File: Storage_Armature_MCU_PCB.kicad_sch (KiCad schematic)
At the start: 58 parts, among them U4 TLV1117LV33DCYR

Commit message: VER1.0: сделал все питание и один измерительный канал
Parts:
- removed C65, C72: 1n, Capacitor_THT:C_Disc_D7.0mm_W2.5mm_P5.00mm, symbol Device:C_Small
- removed C70: 330u, Capacitor_THT:CP_Radial_D10.0mm_P5.00mm, symbol Device:C_Polarized_Small
- removed D21: URB2405ZP-10WR3, MORNSUN:URB_ZP-10WR3, symbol MORNSUN:URB_ZP-10WR3
- removed L3: (no value), Inductor_SMD:L_CommonModeChoke_Murata_DLW5BTMxxxSQ2x_5x5mm, symbol Device:L_Coupled_Small
- added C35, C45, C74: 10u, Capacitor_SMD:C_1206_3216Metric_Pad1.33x1.80mm_HandSolder, symbol Device:C_Small
- added C71, C73: 4.7u, Capacitor_SMD:C_1206_3216Metric_Pad1.33x1.80mm_HandSolder, symbol Device:C_Small
- added D1: B2405S-1WR3, MORNSUN:B_S-1WR3, symbol MORNSUN:B_S-1WR3
- added D10: SMCJ33A, Diode_SMD:D_SMC_Handsoldering, symbol Device:D_TVS
- added D23: (no value), LED_SMD:LED_0805_2012Metric, symbol Device:LED_Small
- added D9: WRB2403S-3WR2, MORNSUN:WRB_S-3WR2, symbol MORNSUN:WRB_S-3WR2
- added L2, L3: 6.8u, Inductor_SMD:L_1210_3225Metric_Pad1.42x2.65mm_HandSolder, symbol Device:L_Small
- added R58: 1.1k, Resistor_SMD:R_0805_2012Metric_Pad1.20x1.40mm_HandSolder, symbol Device:R_Small
- added U5: ADP3338AKCZ-3.3RL7, Package_TO_SOT_SMD:SOT-223-3_TabPin2, symbol Regulator_Linear:LM1117MP-3.3
- C68, C69: value 10u -> 4.7u
- D20: value (none) -> BZT52C10
- F1: value 0451002.MRL -> MF-SM075/60-2; footprint Fuse_my:SMD_2410 -> Fuse:Fuse_Bourns_MF-SM_7.98x5.44mm
- J6: footprint Connector_Molex:Molex_Mini-Fit_Jr_5566-04A_2x02_P4.20mm_Vertical -> Connector_Molex:Molex_Mini-Fit_Jr_5569-04A2_2x02_P4.20mm_Horizontal
- Q1: value (none) -> 20N06
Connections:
- net +24V: now also C67.1, C68.1, F1.2, C73.1, D10.1 (A1), L2.1, L3.1
- net +5V: now also D9.6 (+Vo)
- net -24V: now also D10.2 (A2)
- net GND: now also D9.7 (0V)
- net GNDD: now also C69.2, C71.2, C73.2, D1.1 (GND), D9.1 (GND)
- net GND_CAN: no longer J34.3 (Pin_3), J34.4 (Pin_4), J35.3 (Pin_3), J35.4 (Pin_4)
- net at C69.1: now also D9.2 (Vin), L3.2
- new net: C45.2, C74.1, D1.4 (+Vo), U5.3 (VI)
- new net: J34.3 (Pin_3), J34.4 (Pin_4), J35.3 (Pin_3), J35.4 (Pin_4)
- new net: D23.1 (K), R58.1
- new net: C71.1, D1.2 (Vin), L2.2
- new net +3.3V_ISO: C35.2, D23.2 (A), U5.2 (VO)
- new net GND_ISO: C35.1, C45.1, C74.2, D1.3 (0V), R58.2, U5.1 (GND)
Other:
- added sheet P_measure (Measure.kicad_sch)
- note added: "Защита 24В"
- note added: "Питание 3.3В отвязанное"
- note removed: "Защита от переполюсовки 24В"
- note removed: "НАДО ДОБАВИТЬ VRB2424LD-50WR3 / MORNSUN"
- moved on the sheet: C34, C44, C47, C48, C49, C66, C67, C68, C69, D11, D12, D14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

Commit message: VER1.0: разместил все компоненты
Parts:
- removed D15: (no value), Package_TO_SOT_SMD:SOT-23-3, symbol Power_Protection:ESDA5V3L
- removed H1, H4: MountingHole_Pad, MountingHole:MountingHole_4.3mm_M4_Pad_Via, symbol Mechanical:MountingHole_Pad
- added C65: 100n, Capacitor_SMD:C_0805_2012Metric_Pad1.18x1.45mm_HandSolder, symbol Device:C_Small
- added H4, H5: MountingHole, MountingHole:MountingHole_4.3mm_M4, symbol Mechanical:MountingHole
- added R47, R48: 20, Resistor_SMD:R_0805_2012Metric_Pad1.20x1.40mm_HandSolder, symbol Device:R_Small
- added U14: USBLC6-2P6, Package_TO_SOT_SMD:SOT-23-6, symbol Power_Protection:USBLC6-2SC6
- D5: Product Name BAS416 -> LBAT54HT1G
- J34, J35: footprint Connector_Molex:Molex_Mini-Fit_Jr_5566-04A_2x02_P4.20mm_Vertical -> Connector_Molex:Molex_Mini-Fit_Jr_5569-04A2_2x02_P4.20mm_Horizontal
- R1, R2: value 1k -> 10k
- U4: value TLV1117LV33DCYR -> ADP3338AKCZ-3.3RL7
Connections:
- net CAN1_RXD_MCU is gone; now on net CAN_RXD_MCU: D12.1 (RXD)
- net CAN1_TXD_MCU is gone; now on net CAN_TXD_MCU: D12.2 (TXD)
- net +3.3V: now also U14.5 (VBUS)
- net GND: now also C65.1, U14.2 (GND)
- net GND_CAN: now also J34.3 (Pin_3), J34.4 (Pin_4), J35.3 (Pin_3), J35.4 (Pin_4)
- net NRST: now also C65.2
- net SWCLK: now also U14.1 (I/O1); no longer J1.2 (Pin_2)
- net SWDIO: now also U14.3 (I/O2); no longer J1.3 (Pin_3)
- net CAN_RXD_MCU: now reaches U1.44 (PA11)
- net CAN_TXD_MCU: now reaches U1.45 (PA12)
- new net: R47.1, U14.4 (I/O2)
- new net: R48.1, U14.6 (I/O1)
- new net: J1.2 (Pin_2), R48.2
- new net: J1.3 (Pin_3), R47.2
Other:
- sheet P_measure renamed Sensor_1
- added sheet Sensor_2 (Measure.kicad_sch)
- added sheet Sensor_3 (Measure.kicad_sch)
- added sheet Sensor_4 (Measure.kicad_sch)
- added sheet Sensor_5 (Measure.kicad_sch)
- note removed: "НВЦТ.0001.0400.200_v1"
- note removed: "Разъемы и механические отверстия"
- title: Плата управления -> Плата управления арматурой 
- moved on the sheet: C26, C30, C34, C44, R1, Y1

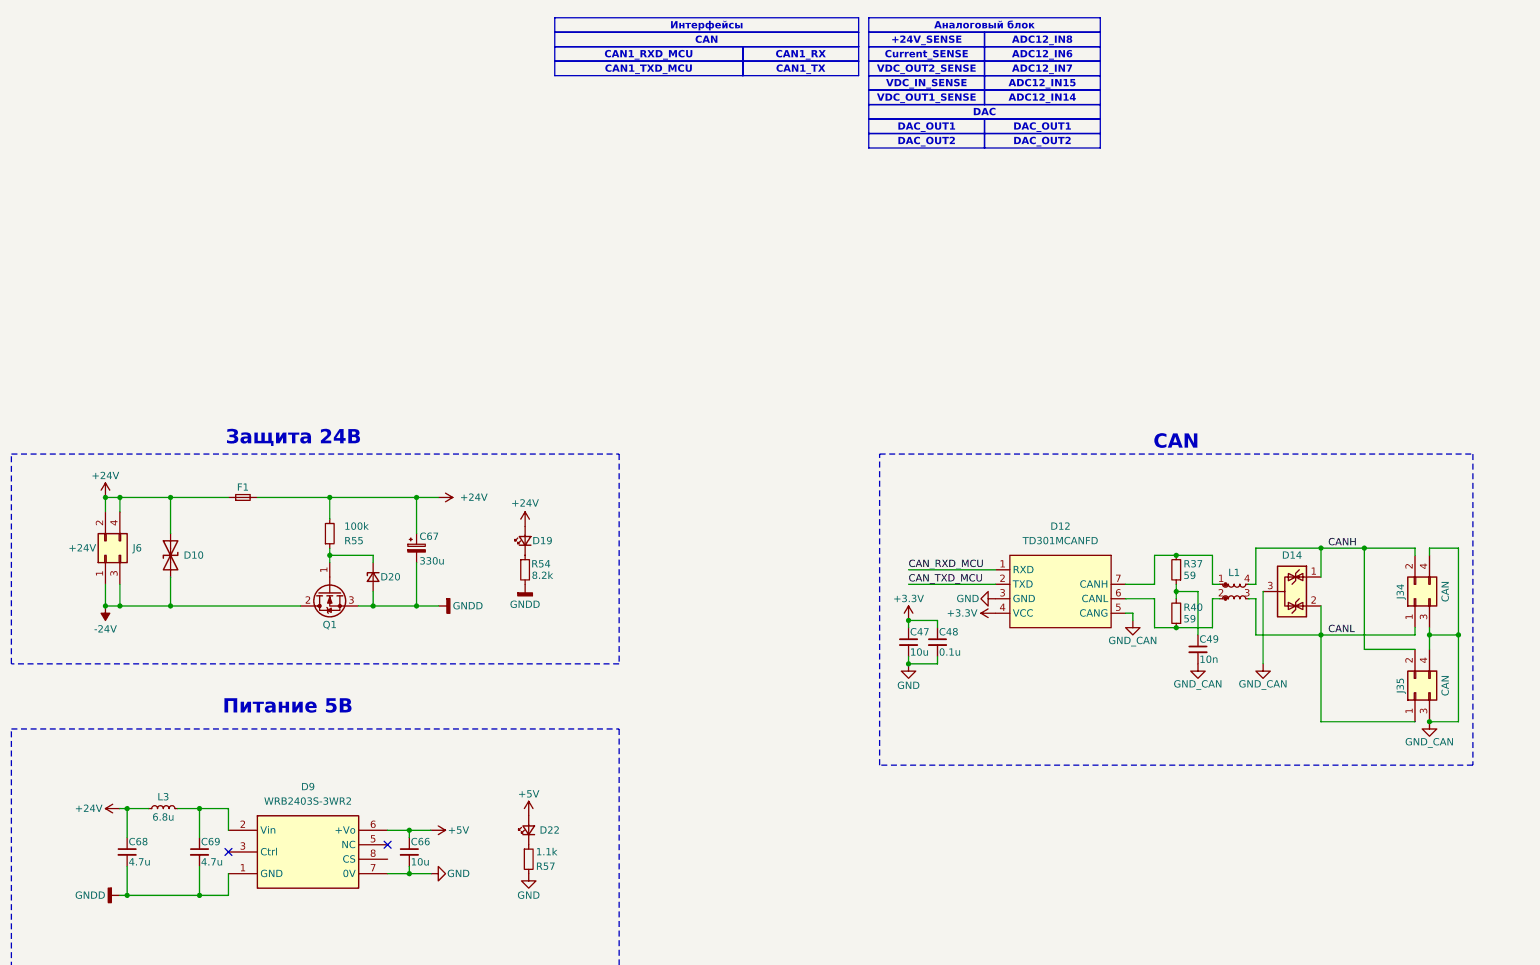
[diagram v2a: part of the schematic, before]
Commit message: VER1.0: развел все кроме ножек МК
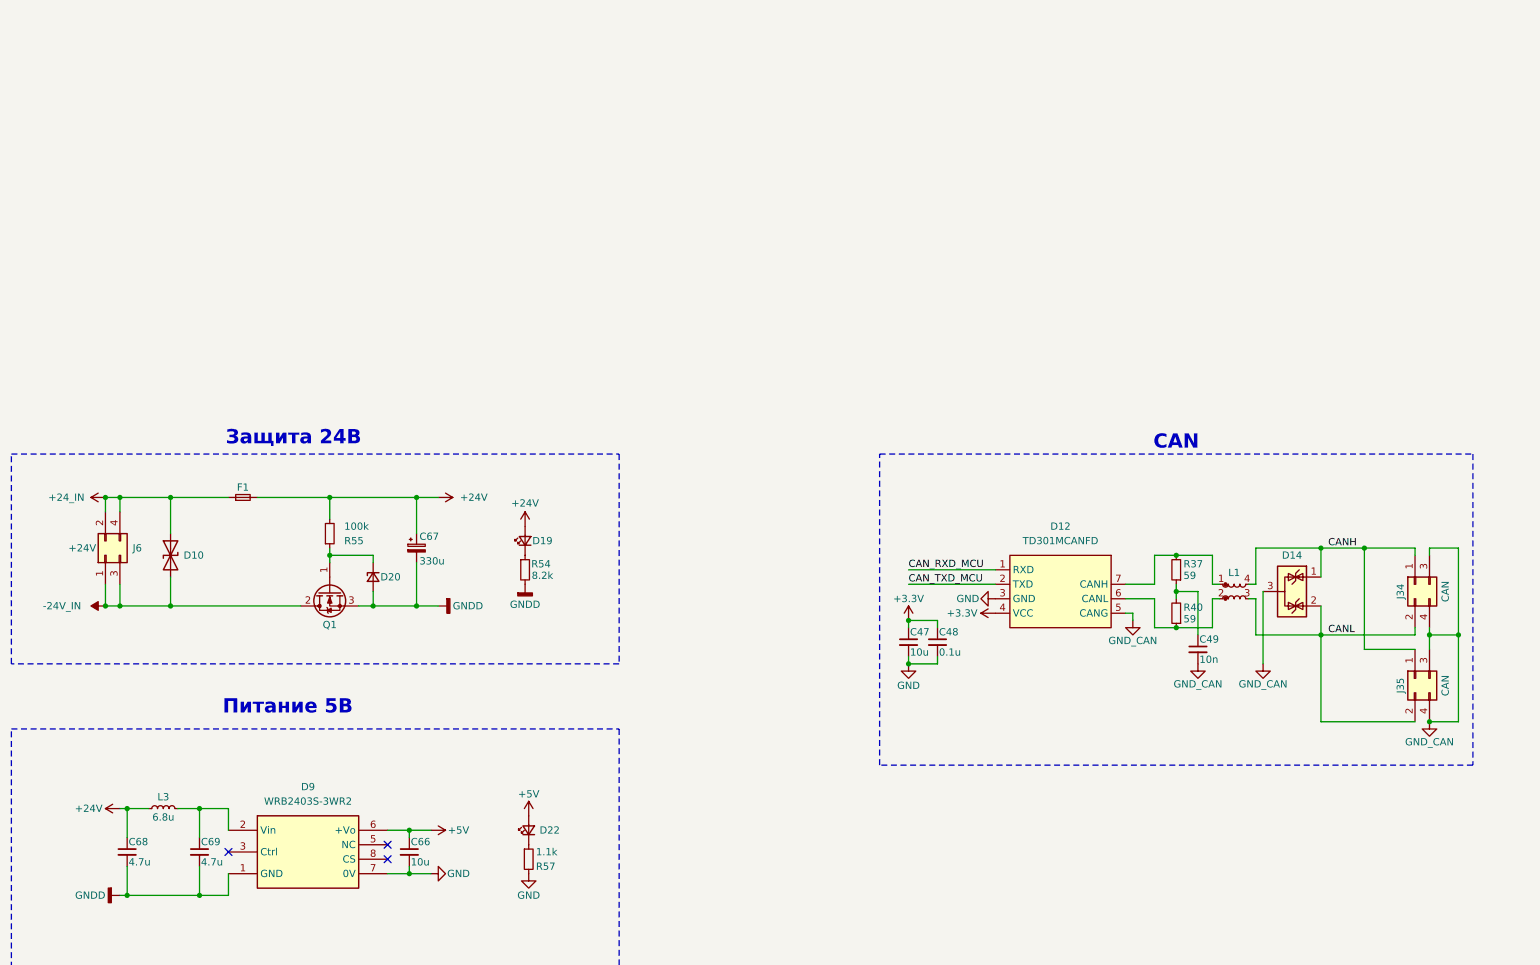
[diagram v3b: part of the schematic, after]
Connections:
- net +24V: no longer D10.1 (A1), F1.1, J6.2 (Pin_2), J6.4 (Pin_4)
- net CANH: now also J34.1 (Pin_1), J35.1 (Pin_1); no longer J34.2 (Pin_2), J35.2 (Pin_2)
- net CANL: now also J34.2 (Pin_2), J35.2 (Pin_2); no longer J34.1 (Pin_1), J35.1 (Pin_1)
- net -24V renamed -24V_IN
- new net +24_IN: D10.1 (A1), F1.1, J6.2 (Pin_2), J6.4 (Pin_4)
- no-connect marks 10 -> 11

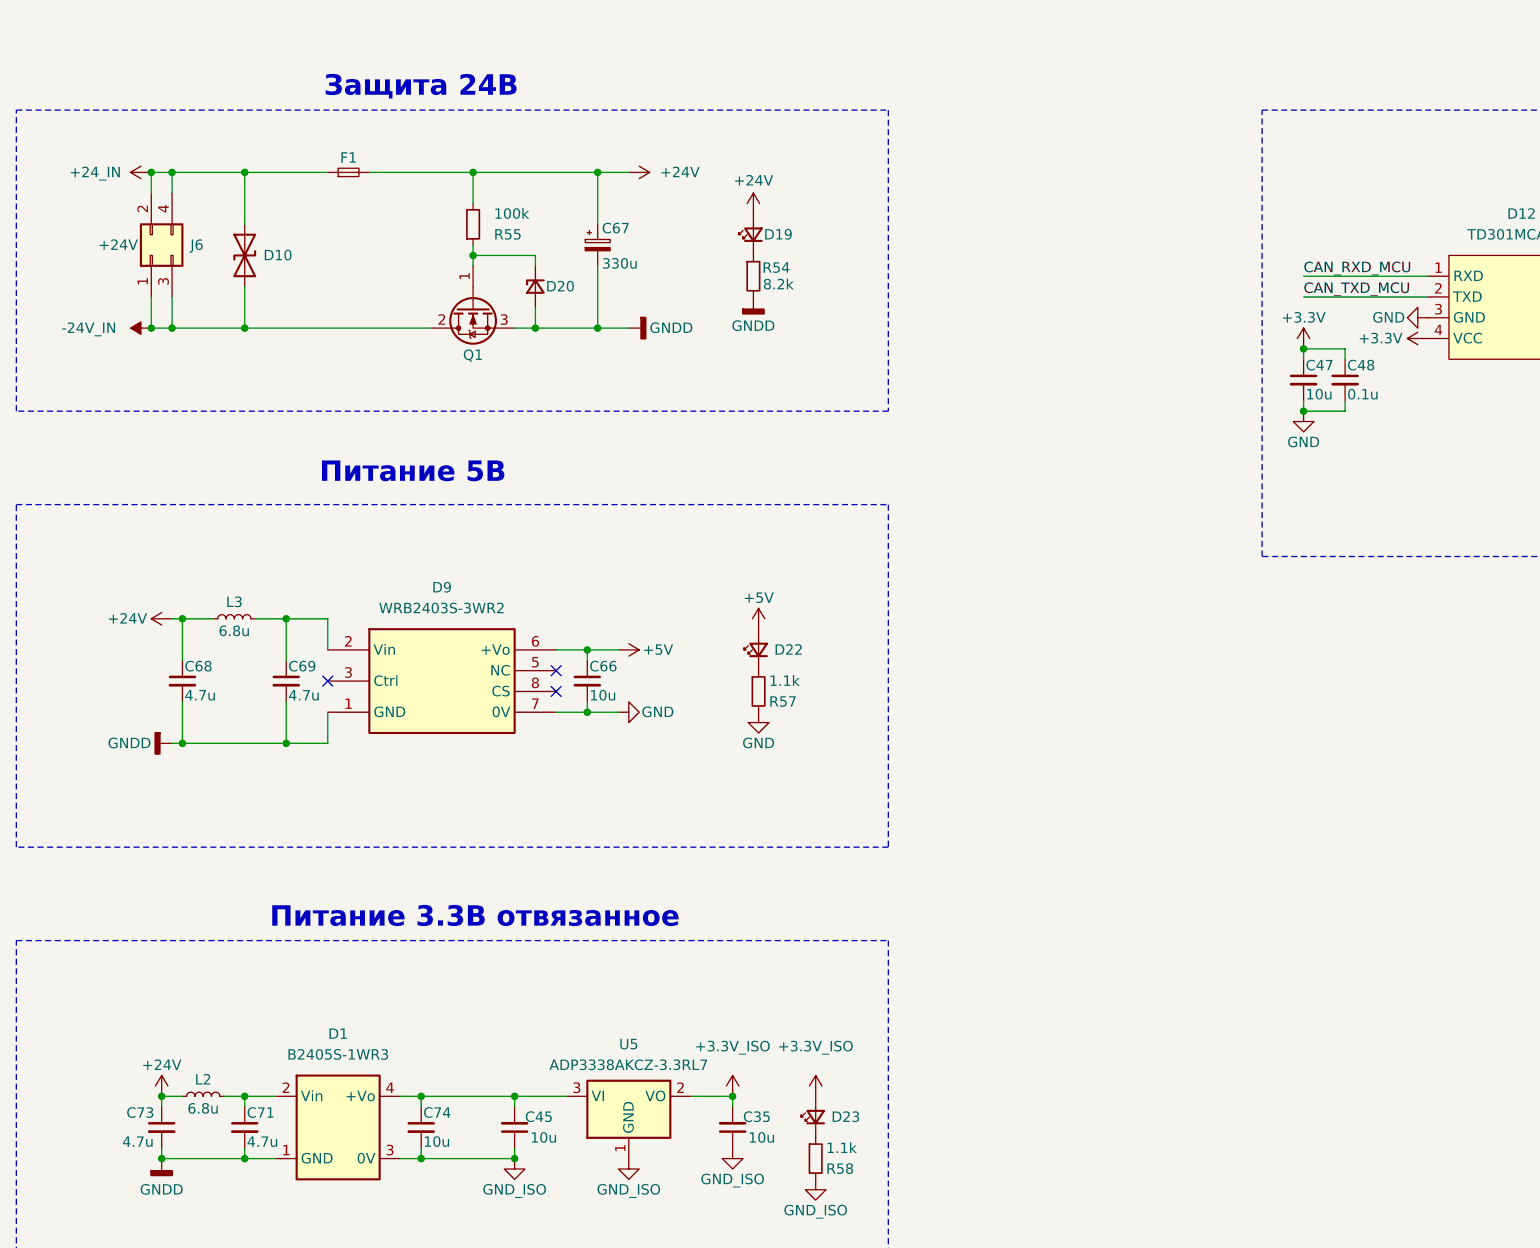
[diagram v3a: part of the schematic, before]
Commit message: VER1.0: добавил предохранители каждому клапану и отдельно по питанию
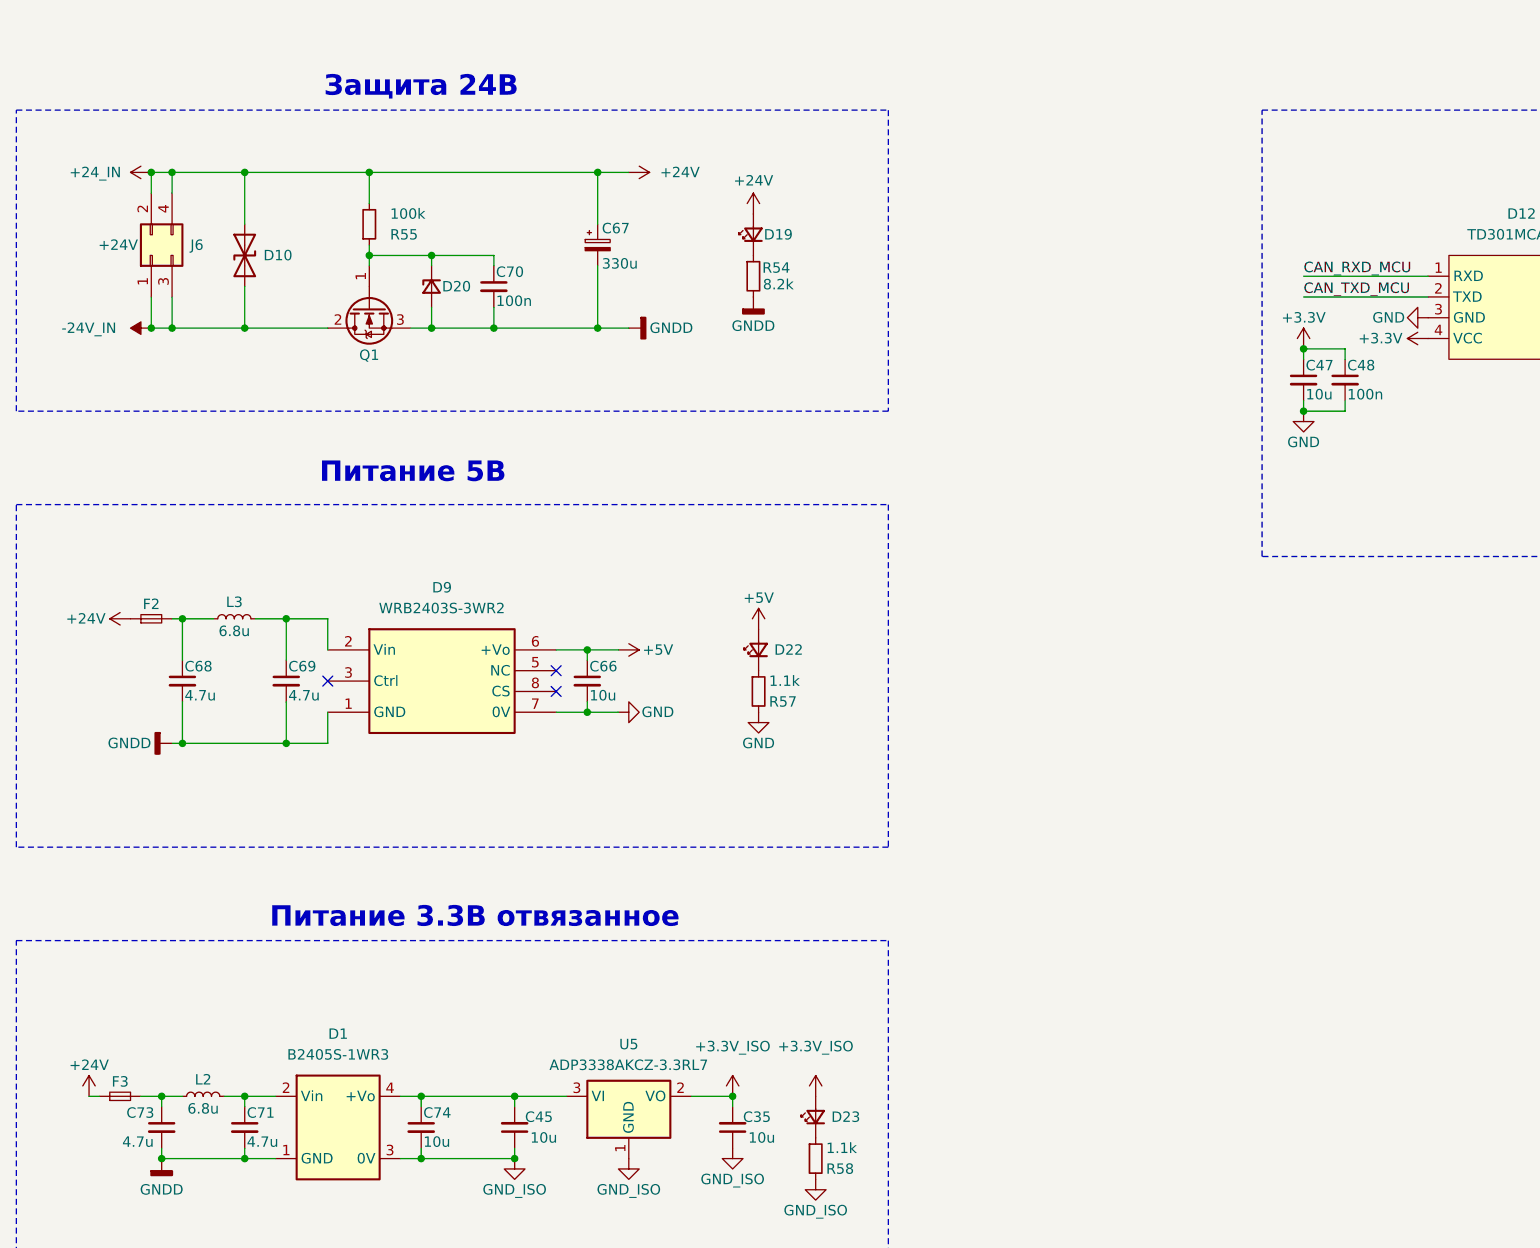
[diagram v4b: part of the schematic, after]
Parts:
- removed F1: MF-SM075/60-2, Fuse:Fuse_Bourns_MF-SM_7.98x5.44mm, symbol Device:Fuse_Small
- added C70: 100n, Capacitor_SMD:C_0805_2012Metric_Pad1.18x1.45mm_HandSolder, symbol Device:C_Small
- added F2: MF-MSMF050/30X-2, Fuse:Fuse_1812_4532Metric, symbol Device:Fuse_Small
- added F3: MF-MSMF020, Fuse:Fuse_1812_4532Metric, symbol Device:Fuse_Small
- C48: value 0.1u -> 100n
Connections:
- net +24_IN is gone; now on net +24V: D10.1 (A1), J6.2 (Pin_2), J6.4 (Pin_4)
- net +24V: now also F2.1, F3.1; no longer C68.1, C73.1, L2.1, L3.1
- net GNDD: now also C70.2
- net at D20.1 (K), Q1.1 (G), R55.1: now also C70.1
- new net: C73.1, F3.2, L2.1
- new net: C68.1, F2.2, L3.1
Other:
- moved on the sheet: D20, Q1, R55
